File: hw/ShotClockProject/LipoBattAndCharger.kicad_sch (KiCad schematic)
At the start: 21 parts, among them IC1 TP4056-42-ESOP8_Rearanged, J4 SM03B-SRSS-TB(LF)(SN)(P), J5 Conn_01x02_Pin, J6 Conn_01x03_Pin, Q1 Q_PMOS_SGD

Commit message: First feedback round from Luc on schematic
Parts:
- removed R7: 1k, Resistor_SMD:R_0402_1005Metric, symbol Device:R
- added C12: 10n, Capacitor_SMD:C_0603_1608Metric, symbol Device:C
- added Q1 (x2): Q_NPN_BCE, Package_TO_SOT_SMD:SOT-23, symbol Device:Q_NPN_BCE
- added R2 (x2): 1k, Resistor_SMD:R_0402_1005Metric, symbol Device:R
- added R2 (x2): 10k, Resistor_SMD:R_0402_1005Metric, symbol Device:R
- added R2: 100k, Resistor_SMD:R_0402_1005Metric, symbol Device:R
- Q1: footprint Package_TO_SOT_SMD:SOT-23 -> (none)
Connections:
- net +BATT: no longer Q1.1 (S)
- net GND: now also C12.2, Q1.3 (E), Q1.3 (E), R2.1, R2.1
- net VBUS: now also R2.2
- net at Q1.2 (G): now also Q1.2 (C), R2.1
- new net: C12.1, Q1.1 (B), R2.1, R2.2
- new net: Q1.1 (B), Q1.2 (C), R2.1, R2.2
- new net: Q1.1 (S), R2.2, R2.2
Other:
- note added: "Voor Q2 fet zoeken die het negatieve van +batt aan kan op de base"
- note removed: "Is it correct to use a P_MOSFET here to shut off the system load (VCC) from the battery. Meaning I can't use the product while charging, but this should give safe charging capabilities. (and the MOSFET is oriented correctly, right?) And with how much R do I limit the MOSFET? How do I calc this? Or is this only needed with transistors, since MOSFETs have high(er) inp. impedance?"
- moved on the sheet: C12, C13, D1, D2, IC1, NT1, R3, R4, R5, R6

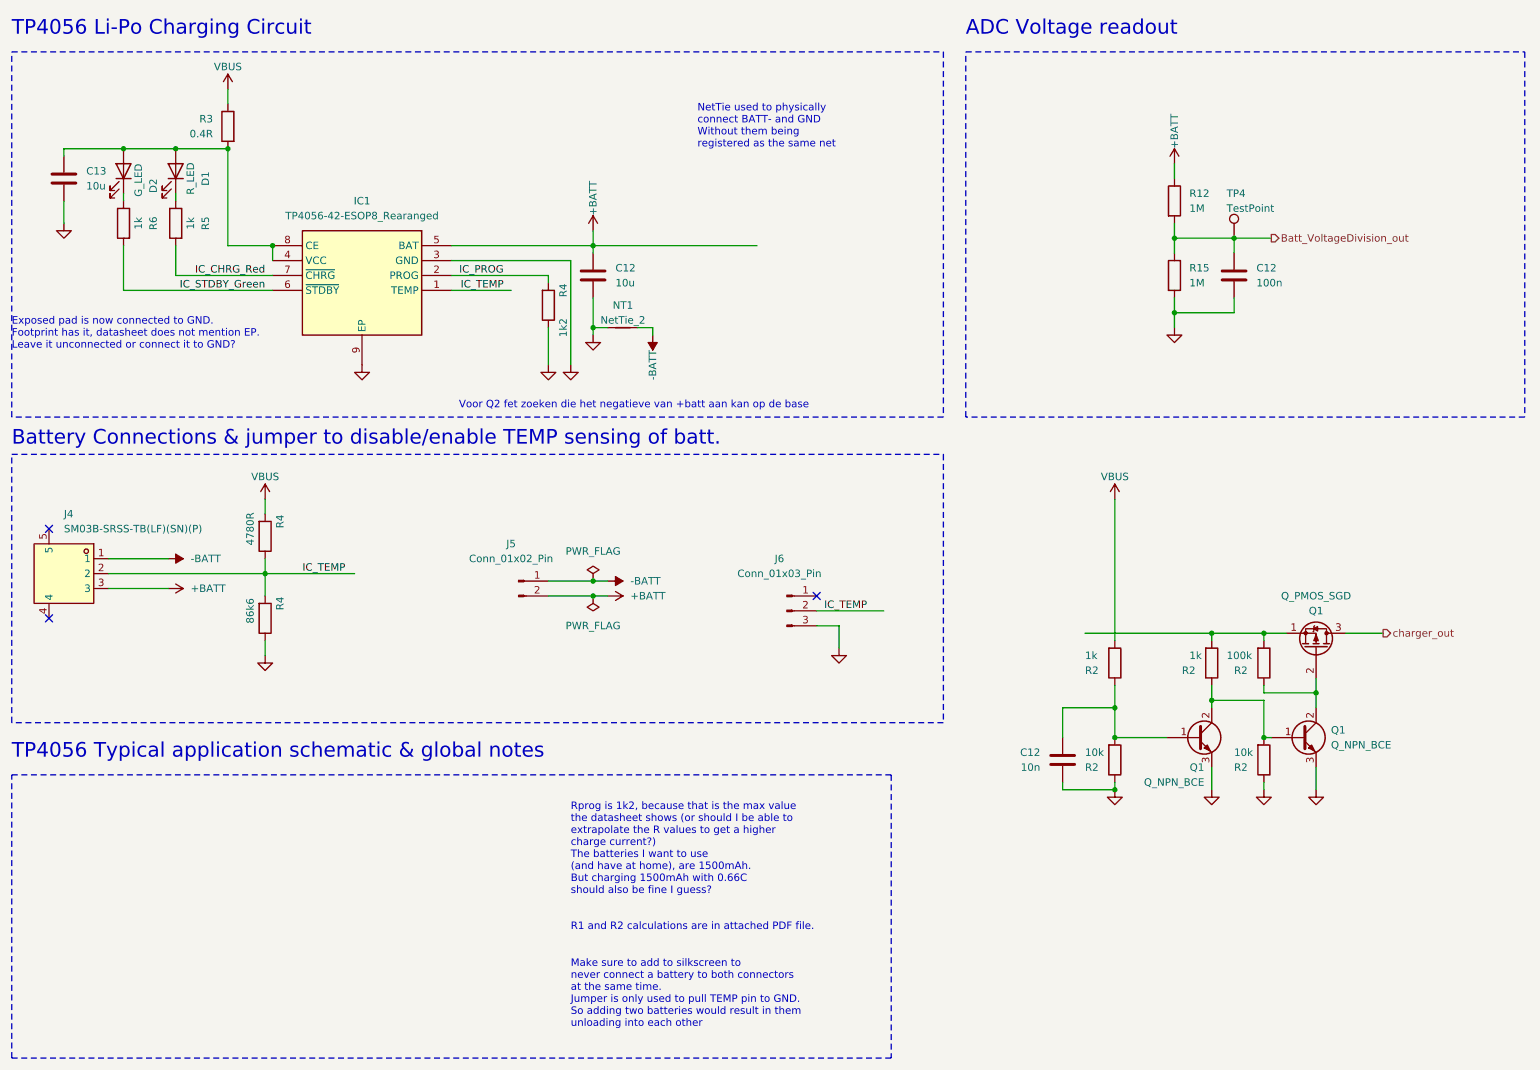
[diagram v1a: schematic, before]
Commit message: Changed pinouts
To only use 1 pwm per display, and GPIo outs for the rest in both HW and firmware
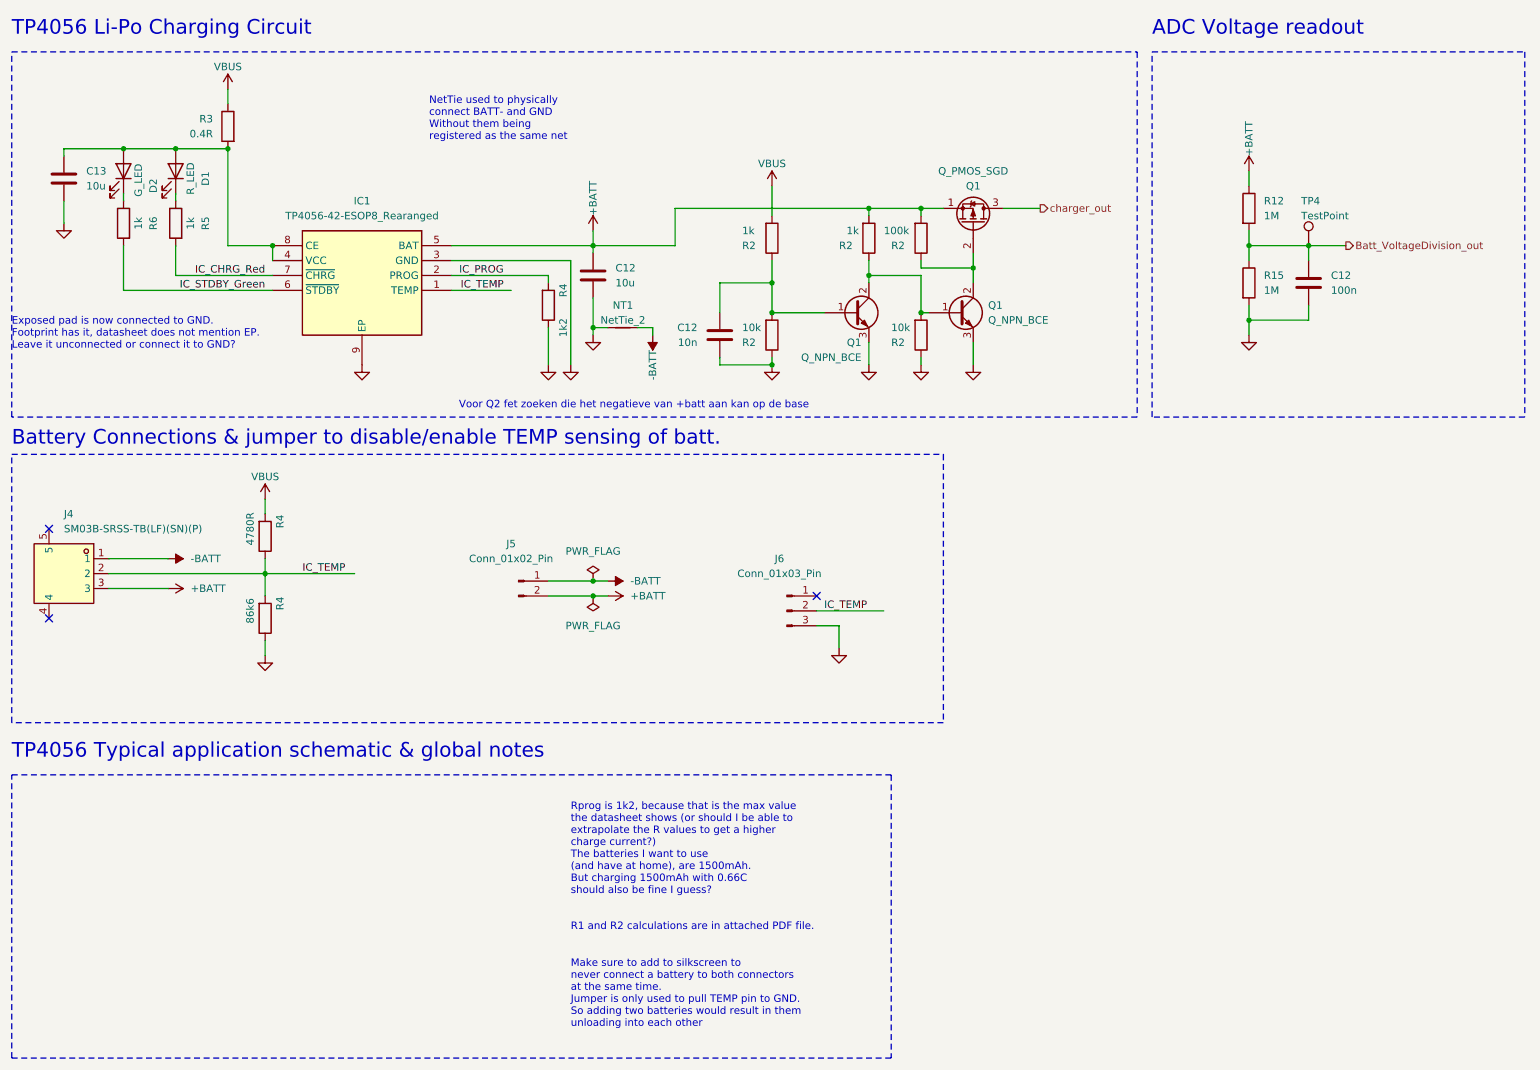
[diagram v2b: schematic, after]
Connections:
- net +BATT: now also Q1.1 (S), R2.2, R2.2
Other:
- moved on the sheet: C12, Q1, R12, R15, R2, TP4

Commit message: Finshed both schematics
- LED driving transistors are placed
- All connectors on segment display PCB are placed
- All schematic references have been re-configured (autosort on Y axis)
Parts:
- renumbered R12 to R14, R15 to R20
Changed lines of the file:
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@@
         )
         (path "/5fd859aa-754d-49c2-9762-3f7ebe3bb64c/d287d155-1951-4d4f-8d6c-570f03bc79f5"
-          (reference "Q2") (unit 1)
+          (reference "Q3") (unit 1)
         )
       )
@@
         )
         (path "/5fd859aa-754d-49c2-9762-3f7ebe3bb64c/d287d155-1951-4d4f-8d6c-570f03bc79f5"
-          (reference "#PWR034") (unit 1)
+          (reference "#PWR037") (unit 1)
         )
       )
@@
         )
         (path "/5fd859aa-754d-49c2-9762-3f7ebe3bb64c/d287d155-1951-4d4f-8d6c-570f03bc79f5"
-          (reference "R13") (unit 1)
+          (reference "R15") (unit 1)
         )
       )
@@
         )
         (path "/5fd859aa-754d-49c2-9762-3f7ebe3bb64c/d287d155-1951-4d4f-8d6c-570f03bc79f5"
-          (reference "#PWR037") (unit 1)
+          (reference "#PWR041") (unit 1)
         )
       )
@@
         )
         (path "/5fd859aa-754d-49c2-9762-3f7ebe3bb64c/d287d155-1951-4d4f-8d6c-570f03bc79f5"
-          (reference "R34") (unit 1)
+          (reference "R17") (unit 1)
         )
       )
@@
         )
         (path "/5fd859aa-754d-49c2-9762-3f7ebe3bb64c/d287d155-1951-4d4f-8d6c-570f03bc79f5"
-          (reference "#PWR039") (unit 1)
+          (reference "#PWR049") (unit 1)
         )
       )
@@
         )
         (path "/5fd859aa-754d-49c2-9762-3f7ebe3bb64c/d287d155-1951-4d4f-8d6c-570f03bc79f5"
-          (reference "#PWR033") (unit 1)
+          (reference "#PWR036") (unit 1)
         )
       )
@@
         )
         (path "/5fd859aa-754d-49c2-9762-3f7ebe3bb64c/d287d155-1951-4d4f-8d6c-570f03bc79f5"
-          (reference "#PWR032") (unit 1)
+          (reference "#PWR038") (unit 1)
         )
       )
@@
         )
         (path "/5fd859aa-754d-49c2-9762-3f7ebe3bb64c/d287d155-1951-4d4f-8d6c-570f03bc79f5"
-          (reference "R30") (unit 1)
+          (reference "R23") (unit 1)
         )
       )
@@
         )
         (path "/5fd859aa-754d-49c2-9762-3f7ebe3bb64c/d287d155-1951-4d4f-8d6c-570f03bc79f5"
-          (reference "#PWR076") (unit 1)
+          (reference "#PWR033") (unit 1)
         )
       )
@@
         )
         (path "/5fd859aa-754d-49c2-9762-3f7ebe3bb64c/d287d155-1951-4d4f-8d6c-570f03bc79f5"
-          (reference "Q4") (unit 1)
+          (reference "Q2") (unit 1)
         )
       )
@@
         )
         (path "/5fd859aa-754d-49c2-9762-3f7ebe3bb64c/d287d155-1951-4d4f-8d6c-570f03bc79f5"
-          (reference "#PWR030") (unit 1)
+          (reference "#PWR034") (unit 1)
         )
       )
@@
         )
         (path "/5fd859aa-754d-49c2-9762-3f7ebe3bb64c/d287d155-1951-4d4f-8d6c-570f03bc79f5"
-          (reference "#PWR079") (unit 1)
+          (reference "#PWR042") (unit 1)
         )
       )
@@
         )
         (path "/5fd859aa-754d-49c2-9762-3f7ebe3bb64c/d287d155-1951-4d4f-8d6c-570f03bc79f5"
-          (reference "#PWR036") (unit 1)
+          (reference "#PWR040") (unit 1)
         )
       )
@@
         )
         (path "/5fd859aa-754d-49c2-9762-3f7ebe3bb64c/d287d155-1951-4d4f-8d6c-570f03bc79f5"
-          (reference "#PWR038") (unit 1)
+          (reference "#PWR046") (unit 1)
         )
       )
@@
         )
         (path "/5fd859aa-754d-49c2-9762-3f7ebe3bb64c/d287d155-1951-4d4f-8d6c-570f03bc79f5"
-          (reference "#PWR035") (unit 1)
+          (reference "#PWR039") (unit 1)
         )
       )
@@
         )
         (path "/5fd859aa-754d-49c2-9762-3f7ebe3bb64c/d287d155-1951-4d4f-8d6c-570f03bc79f5"
-          (reference "#PWR028") (unit 1)
+          (reference "#PWR031") (unit 1)
         )
       )
@@
         )
         (path "/5fd859aa-754d-49c2-9762-3f7ebe3bb64c/d287d155-1951-4d4f-8d6c-570f03bc79f5"
-          (reference "C16") (unit 1)
+          (reference "C15") (unit 1)
         )
       )
@@
         )
         (path "/5fd859aa-754d-49c2-9762-3f7ebe3bb64c/d287d155-1951-4d4f-8d6c-570f03bc79f5"
-          (reference "R18") (unit 1)
+          (reference "R25") (unit 1)
         )
       )
@@
         )
         (path "/5fd859aa-754d-49c2-9762-3f7ebe3bb64c/d287d155-1951-4d4f-8d6c-570f03bc79f5"
-          (reference "R10") (unit 1)
+          (reference "R13") (unit 1)
         )
       )
@@
         )
         (path "/5fd859aa-754d-49c2-9762-3f7ebe3bb64c/d287d155-1951-4d4f-8d6c-570f03bc79f5"
-          (reference "C25") (unit 1)
+          (reference "C17") (unit 1)
         )
       )
@@
         )
         (path "/5fd859aa-754d-49c2-9762-3f7ebe3bb64c/d287d155-1951-4d4f-8d6c-570f03bc79f5"
-          (reference "#PWR043") (unit 1)
+          (reference "#PWR051") (unit 1)
         )
       )
@@
         )
         (path "/5fd859aa-754d-49c2-9762-3f7ebe3bb64c/d287d155-1951-4d4f-8d6c-570f03bc79f5"
-          (reference "R16") (unit 1)
+          (reference "R21") (unit 1)
         )
       )
@@
         )
         (path "/5fd859aa-754d-49c2-9762-3f7ebe3bb64c/d287d155-1951-4d4f-8d6c-570f03bc79f5"
-          (reference "#PWR040") (unit 1)
+          (reference "#PWR050") (unit 1)
         )
       )
@@
         )
         (path "/5fd859aa-754d-49c2-9762-3f7ebe3bb64c/d287d155-1951-4d4f-8d6c-570f03bc79f5"
-          (reference "TP11") (unit 1)
+          (reference "TP12") (unit 1)
         )
       )
@@
         )
         (path "/5fd859aa-754d-49c2-9762-3f7ebe3bb64c/d287d155-1951-4d4f-8d6c-570f03bc79f5"
-          (reference "R31") (unit 1)
+          (reference "R19") (unit 1)
         )
       )
@@
         )
         (path "/5fd859aa-754d-49c2-9762-3f7ebe3bb64c/d287d155-1951-4d4f-8d6c-570f03bc79f5"
-          (reference "R17") (unit 1)
+          (reference "R24") (unit 1)
         )
       )
@@
         )
         (path "/5fd859aa-754d-49c2-9762-3f7ebe3bb64c/d287d155-1951-4d4f-8d6c-570f03bc79f5"
-          (reference "#PWR078") (unit 1)
+          (reference "#PWR045") (unit 1)
         )
       )
@@
         )
         (path "/5fd859aa-754d-49c2-9762-3f7ebe3bb64c/d287d155-1951-4d4f-8d6c-570f03bc79f5"
-          (reference "#PWR029") (unit 1)
+          (reference "#PWR032") (unit 1)
         )
       )
@@
         )
         (path "/5fd859aa-754d-49c2-9762-3f7ebe3bb64c/d287d155-1951-4d4f-8d6c-570f03bc79f5"
-          (reference "#PWR041") (unit 1)
+          (reference "#PWR047") (unit 1)
         )
       )
@@
   (symbol (lib_id "Device:R") (at 233.68 49.53 0) (unit 1)
     (in_bom yes) (on_board yes) (dnp no) (fields_autoplaced)
-    (property "Reference" "R12" (at 236.22 48.26 0)
+    (property "Reference" "R14" (at 236.22 48.26 0)
       (effects (font (size 1.27 1.27)) (justify left))
     )
@@
       (project "ShotClockProject"
         (path "/5fd859aa-754d-49c2-9762-3f7ebe3bb64c/d287d155-1951-4d4f-8d6c-570f03bc79f5"
-          (reference "R12") (unit 1)
+          (reference "R14") (unit 1)
         )
       )
@@
         )
         (path "/5fd859aa-754d-49c2-9762-3f7ebe3bb64c/d287d155-1951-4d4f-8d6c-570f03bc79f5"
-          (reference "#PWR031") (unit 1)
+          (reference "#PWR035") (unit 1)
         )
       )
@@
         )
         (path "/5fd859aa-754d-49c2-9762-3f7ebe3bb64c/d287d155-1951-4d4f-8d6c-570f03bc79f5"
-          (reference "R32") (unit 1)
+          (reference "R18") (unit 1)
         )
       )
@@
         )
         (path "/5fd859aa-754d-49c2-9762-3f7ebe3bb64c/d287d155-1951-4d4f-8d6c-570f03bc79f5"
-          (reference "#PWR077") (unit 1)
+          (reference "#PWR044") (unit 1)
         )
       )
@@
         )
         (path "/5fd859aa-754d-49c2-9762-3f7ebe3bb64c/d287d155-1951-4d4f-8d6c-570f03bc79f5"
-          (reference "Q3") (unit 1)
+          (reference "Q4") (unit 1)
         )
       )
@@
         )
         (path "/5fd859aa-754d-49c2-9762-3f7ebe3bb64c/d287d155-1951-4d4f-8d6c-570f03bc79f5"
-          (reference "R14") (unit 1)
+          (reference "R16") (unit 1)
         )
       )
@@
         )
         (path "/5fd859aa-754d-49c2-9762-3f7ebe3bb64c/d287d155-1951-4d4f-8d6c-570f03bc79f5"
-          (reference "#PWR042") (unit 1)
+          (reference "#PWR048") (unit 1)
         )
       )
@@
         )
         (path "/5fd859aa-754d-49c2-9762-3f7ebe3bb64c/d287d155-1951-4d4f-8d6c-570f03bc79f5"
-          (reference "#FLG06") (unit 1)
+          (reference "#FLG07") (unit 1)
         )
         (path "/5fd859aa-754d-49c2-9762-3f7ebe3bb64c/17367eb9-0f4d-4017-b1ca-d50430410a5d"
@@
         )
         (path "/5fd859aa-754d-49c2-9762-3f7ebe3bb64c/d287d155-1951-4d4f-8d6c-570f03bc79f5"
-          (reference "#PWR080") (unit 1)
+          (reference "#PWR043") (unit 1)
         )
       )
@@
         )
         (path "/5fd859aa-754d-49c2-9762-3f7ebe3bb64c/d287d155-1951-4d4f-8d6c-570f03bc79f5"
-          (reference "#FLG05") (unit 1)
+          (reference "#FLG06") (unit 1)
         )
       )
@@
         )
         (path "/5fd859aa-754d-49c2-9762-3f7ebe3bb64c/d287d155-1951-4d4f-8d6c-570f03bc79f5"
-          (reference "C15") (unit 1)
+          (reference "C16") (unit 1)
         )
       )
@@
         )
         (path "/5fd859aa-754d-49c2-9762-3f7ebe3bb64c/d287d155-1951-4d4f-8d6c-570f03bc79f5"
-          (reference "#PWR044") (unit 1)
+          (reference "#PWR052") (unit 1)
         )
       )
@@
         )
         (path "/5fd859aa-754d-49c2-9762-3f7ebe3bb64c/d287d155-1951-4d4f-8d6c-570f03bc79f5"
-          (reference "R33") (unit 1)
+          (reference "R22") (unit 1)
         )
       )
@@
   (symbol (lib_id "Device:R") (at 233.68 62.23 0) (unit 1)
     (in_bom yes) (on_board yes) (dnp no) (fields_autoplaced)
-    (property "Reference" "R15" (at 236.22 60.96 0)
+    (property "Reference" "R20" (at 236.22 60.96 0)
       (effects (font (size 1.27 1.27)) (justify left))
     )
@@
       (project "ShotClockProject"
         (path "/5fd859aa-754d-49c2-9762-3f7ebe3bb64c/d287d155-1951-4d4f-8d6c-570f03bc79f5"
-          (reference "R15") (unit 1)
-        )
-      )
+          (reference "R20") (unit 1)
+        )
+      )

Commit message: Added footprint for MOSFET and updated PCB
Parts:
- Q1: footprint (none) -> Package_TO_SOT_SMD:TO-263-2
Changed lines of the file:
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@@
       (effects (font (size 1.27 1.27)))
     )
-    (property "Footprint" "" (at 189.23 46.99 0)
+    (property "Footprint" "Package_TO_SOT_SMD:TO-263-2" (at 189.23 46.99 0)
       (effects (font (size 1.27 1.27)) hide)
     )

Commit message: Redid layout with new board dimensions
Changed tactile switches to larger push switches (also momentary)
Changed USART1 to UART4 & added UART5 to STDC14 connector
Placed all components nearer to each other, and within the PCB outer edge
Added rounded corners
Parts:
- TP4: footprint TestPoint:TestPoint_Pad_D2.5mm -> TestPoint:TestPoint_Pad_D1.0mm
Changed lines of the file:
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@@
       (effects (font (size 1.27 1.27)) (justify left))
     )
-    (property "Footprint" "TestPoint:TestPoint_Pad_D2.5mm" (at 248.92 55.88 0)
+    (property "Footprint" "TestPoint:TestPoint_Pad_D1.0mm" (at 248.92 55.88 0)
       (effects (font (size 1.27 1.27)) hide)
     )
